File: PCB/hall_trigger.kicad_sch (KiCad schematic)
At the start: 2 parts

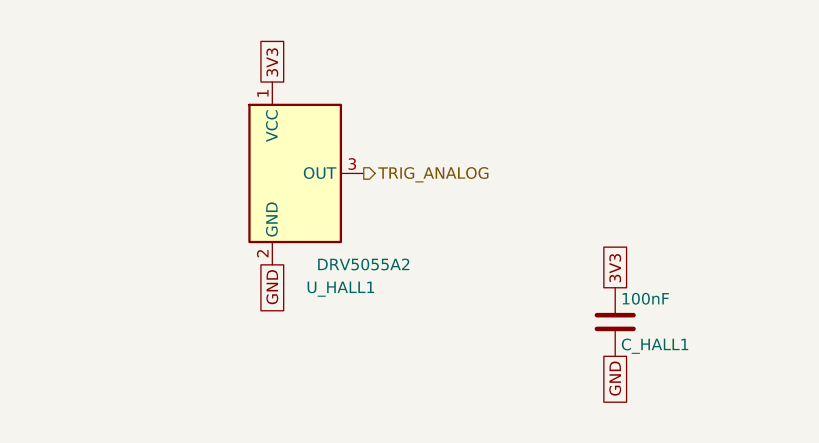
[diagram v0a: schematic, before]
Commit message: Fix footprints and begin layout (#17)
* refactor: updated gulikit footprint

This updates the gulikit thumbstick footprint to be accurate.

* layout: beginning pcb layout

This updates the schematic with a few different footprints while also starts the layout.
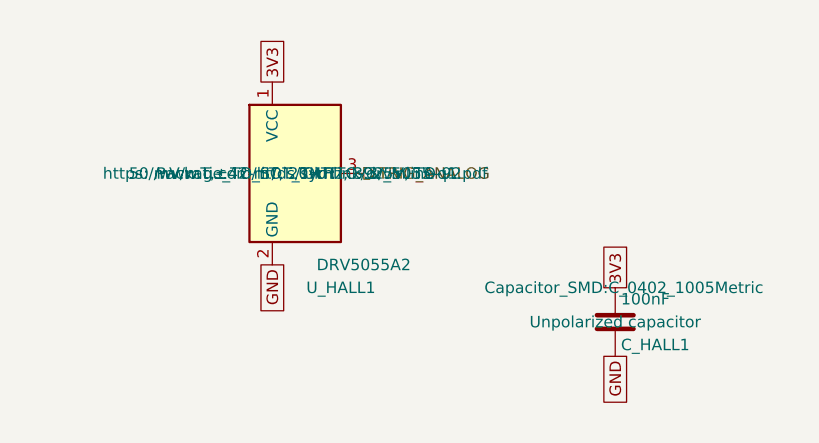
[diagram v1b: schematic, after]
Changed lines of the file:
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@@
 	(generator_version "10.0")
 	(paper "A4")
+	(global_label "3V3"
+		(shape passive)
+		(at 166.37 109.22 90)
+		(fields_autoplaced yes)
+		(effects
+			(font
+				(size 1.27 1.27)
+			)
+			(justify left)
+		)
+		(property "Intersheetrefs" "${INTERSHEET_REFS}"
+			(at 166.37 109.22 0)
+			(hide yes)
+			(show_name no)
+			(do_not_autoplace no)
+			(effects
+				(font
+					(size 1.27 1.27)
+				)
+			)
+		)
+	)
 	(global_label "GND"
 		(shape passive)
+		(at 128.27 106.68 270)
+		(fields_autoplaced yes)
+		(effects
+			(font
+				(size 1.27 1.27)
+			)
+			(justify right)
+		)
+		(property "Intersheetrefs" "${INTERSHEET_REFS}"
+			(at 128.27 106.68 0)
+			(hide yes)
+			(show_name no)
+			(do_not_autoplace no)
+			(effects
+				(font
+					(size 1.27 1.27)
+				)
+			)
+		)
+	)
+	(global_label "GND"
+		(shape passive)
 		(at 166.37 116.84 270)
 		(fields_autoplaced yes)
@@
 		(property "Intersheetrefs" "${INTERSHEET_REFS}"
 			(at 166.37 116.84 0)
-			(hide yes)
-			(show_name no)
-			(do_not_autoplace no)
-			(effects
-				(font
-					(size 1.27 1.27)
-				)
-			)
-		)
-	)
-	(global_label "3V3"
-		(shape passive)
-		(at 166.37 109.22 90)
-		(fields_autoplaced yes)
-		(effects
-			(font
-				(size 1.27 1.27)
-			)
-			(justify left)
-		)
-		(property "Intersheetrefs" "${INTERSHEET_REFS}"
-			(at 166.37 109.22 0)
-			(hide yes)
-			(show_name no)
-			(do_not_autoplace no)
-			(effects
-				(font
-					(size 1.27 1.27)
-				)
-			)
-		)
-	)
-	(global_label "GND"
-		(shape passive)
-		(at 128.27 106.68 270)
-		(fields_autoplaced yes)
-		(effects
-			(font
-				(size 1.27 1.27)
-			)
-			(justify right)
-		)
-		(property "Intersheetrefs" "${INTERSHEET_REFS}"
-			(at 128.27 106.68 0)
 			(hide yes)
 			(show_name no)
@@
 		(property "Footprint" "Capacitor_SMD:C_0402_1005Metric"
 			(at 167.3352 109.22 0)
-			(hide yes)
 			(show_name no)
 			(do_not_autoplace no)
@@
 		(property "Datasheet" ""
 			(at 166.37 113.03 0)
-			(hide yes)
 			(show_name no)
 			(do_not_autoplace no)
@@
 		(property "Description" "Unpolarized capacitor"
 			(at 166.37 113.03 0)
-			(hide yes)
 			(show_name no)
 			(do_not_autoplace no)
@@
 		(instances
 			(project "snips_controller"
-				(path "/868f8289-8434-4465-b2f4-2accc5e40bab/3b2478ec-2890-4ec8-b56f-d58b64ce58ab"
+				(path "/868f8289-8434-4465-b2f4-2accc5e40bab/58aa3fea-7023-42af-afb1-45eaa756099e"
 					(reference "C_HALL1")
+					(unit 1)
+				)
+			)
+			(project ""
+				(path "/d0f5b7d7-b2b6-4492-958c-e60265d3c6b4/58aa3fea-7023-42af-afb1-45eaa756099e"
+					(reference "C_HALL")
 					(unit 1)
 				)
@@
 		(property "Footprint" "Package_TO_SOT_THT:TO-92_Inline"
 			(at 130.81 96.52 0)
-			(hide yes)
 			(show_name no)
 			(do_not_autoplace no)
@@
 		(property "Datasheet" "https://www.ti.com/lit/ds/symlink/drv5055-q1.pdf"
 			(at 130.81 96.52 0)
-			(hide yes)
 			(show_name no)
 			(do_not_autoplace no)
@@
 		(property "Description" "50 mV/mT,±42-mT, 20-kHz, 3.3/5V, TO-92"
 			(at 130.81 96.52 0)
-			(hide yes)
 			(show_name no)
 			(do_not_autoplace no)
@@
 		(instances
 			(project "snips_controller"
-				(path "/868f8289-8434-4465-b2f4-2accc5e40bab/3b2478ec-2890-4ec8-b56f-d58b64ce58ab"
+				(path "/868f8289-8434-4465-b2f4-2accc5e40bab/58aa3fea-7023-42af-afb1-45eaa756099e"
 					(reference "U_HALL1")
 					(unit 1)
 				)
+			)
+			(project ""
+				(path "/d0f5b7d7-b2b6-4492-958c-e60265d3c6b4/58aa3fea-7023-42af-afb1-45eaa756099e"
+					(reference "U_HALL")
+					(unit 1)
+				)

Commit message: refactor: swap footprints and add symmetry
This updates the footprints of a couple components to be smaller and closer to what we want. It also adds two buttons to ensure left and right side symmetry.
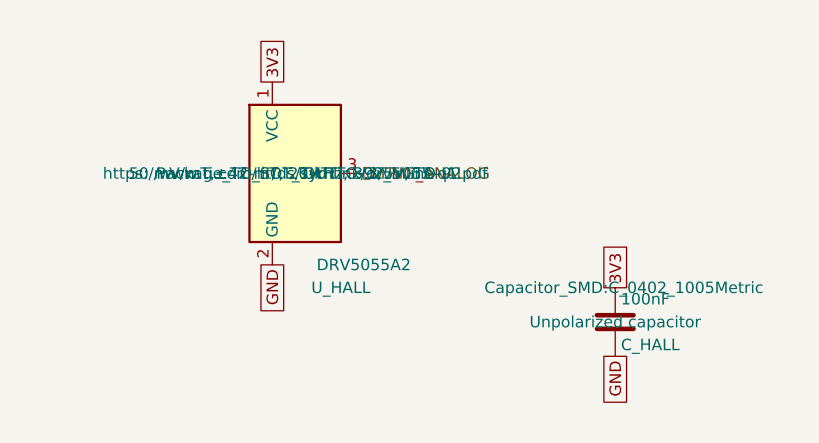
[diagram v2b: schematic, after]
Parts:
- removed C_HALL1: 100nF, Capacitor_SMD:C_0402_1005Metric, symbol Device:C
- removed U_HALL1: DRV5055A2, Package_TO_SOT_THT:TO-92_Inline, symbol Sensor_Magnetic:DRV5055A2xLPGxQ1
- added C_HALL: 100nF, Capacitor_SMD:C_0402_1005Metric, symbol Device:C
- added U_HALL: DRV5055A2, Package_TO_SOT_THT:TO-92_Inline, symbol Sensor_Magnetic:DRV5055A2xLPGxQ1
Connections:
- net 3V3: now also C_HALL.1, U_HALL.1 (VCC)
- net GND: now also C_HALL.2, U_HALL.2 (GND)
- net TRIG_ANALOG: now also U_HALL.3 (OUT)
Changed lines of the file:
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@@
 		(dnp no)
 		(fields_autoplaced yes)
-		(property "Reference" "C_HALL1"
+		(property "Reference" "C_HALL"
 			(at 167.005 115.57 0)
 			(show_name no)
@@
 		(instances
 			(project "snips_controller"
-				(path "/868f8289-8434-4465-b2f4-2accc5e40bab/58aa3fea-7023-42af-afb1-45eaa756099e"
-					(reference "C_HALL1")
-					(unit 1)
-				)
-			)
-			(project ""
-				(path "/d0f5b7d7-b2b6-4492-958c-e60265d3c6b4/58aa3fea-7023-42af-afb1-45eaa756099e"
+				(path "/f9d779c6-e1a6-4677-9004-6e9cc3d2fa8d/8effc149-159c-4301-a85e-5bb660fe4c99"
 					(reference "C_HALL")
 					(unit 1)
@@
 		(dnp no)
 		(fields_autoplaced yes)
-		(property "Reference" "U_HALL1"
+		(property "Reference" "U_HALL"
 			(at 135.89 109.22 0)
 			(show_name no)
@@
 		(instances
 			(project "snips_controller"
-				(path "/868f8289-8434-4465-b2f4-2accc5e40bab/58aa3fea-7023-42af-afb1-45eaa756099e"
-					(reference "U_HALL1")
-					(unit 1)
-				)
-			)
-			(project ""
-				(path "/d0f5b7d7-b2b6-4492-958c-e60265d3c6b4/58aa3fea-7023-42af-afb1-45eaa756099e"
+				(path "/f9d779c6-e1a6-4677-9004-6e9cc3d2fa8d/8effc149-159c-4301-a85e-5bb660fe4c99"
 					(reference "U_HALL")
 					(unit 1)

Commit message: layout: everything is on the board
The board edge cuts are down to 100mm x 35mm. All the components have the right footprints and are on the board, but no traces exist yet, and not all circuits are laid out properly yet. Lots of DRC warnings.
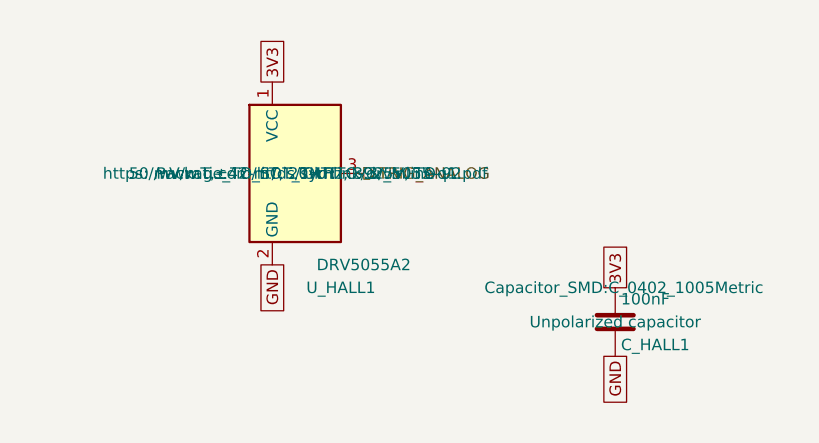
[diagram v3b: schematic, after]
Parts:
- removed C_HALL: 100nF, Capacitor_SMD:C_0402_1005Metric, symbol Device:C
- removed U_HALL: DRV5055A2, Package_TO_SOT_THT:TO-92_Inline, symbol Sensor_Magnetic:DRV5055A2xLPGxQ1
- added C_HALL1: 100nF, Capacitor_SMD:C_0402_1005Metric, symbol Device:C
- added U_HALL1: DRV5055A2, Package_TO_SOT_THT:TO-92_Inline, symbol Sensor_Magnetic:DRV5055A2xLPGxQ1
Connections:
- net 3V3: now also C_HALL1.1, U_HALL1.1 (VCC)
- net GND: now also C_HALL1.2, U_HALL1.2 (GND)
- net TRIG_ANALOG: now also U_HALL1.3 (OUT)
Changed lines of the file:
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@@
 	(generator_version "10.0")
 	(paper "A4")
+	(global_label "GND"
+		(shape passive)
+		(at 128.27 106.68 270)
+		(fields_autoplaced yes)
+		(effects
+			(font
+				(size 1.27 1.27)
+			)
+			(justify right)
+		)
+		(property "Intersheetrefs" "${INTERSHEET_REFS}"
+			(at 128.27 106.68 0)
+			(hide yes)
+			(show_name no)
+			(do_not_autoplace no)
+			(effects
+				(font
+					(size 1.27 1.27)
+				)
+			)
+		)
+	)
 	(global_label "3V3"
 		(shape passive)
@@
 		(property "Intersheetrefs" "${INTERSHEET_REFS}"
 			(at 166.37 109.22 0)
-			(hide yes)
-			(show_name no)
-			(do_not_autoplace no)
-			(effects
-				(font
-					(size 1.27 1.27)
-				)
-			)
-		)
-	)
-	(global_label "GND"
-		(shape passive)
-		(at 128.27 106.68 270)
-		(fields_autoplaced yes)
-		(effects
-			(font
-				(size 1.27 1.27)
-			)
-			(justify right)
-		)
-		(property "Intersheetrefs" "${INTERSHEET_REFS}"
-			(at 128.27 106.68 0)
 			(hide yes)
 			(show_name no)
@@
 			)
 			(justify left)
+		)
+	)
+	(symbol
+		(lib_id "Sensor_Magnetic:DRV5055A2xLPGxQ1")
+		(at 130.81 96.52 0)
+		(unit 1)
+		(body_style 1)
+		(exclude_from_sim no)
+		(in_bom yes)
+		(on_board yes)
+		(in_pos_files yes)
+		(dnp no)
+		(fields_autoplaced yes)
+		(property "Reference" "U_HALL1"
+			(at 135.89 109.22 0)
+			(show_name no)
+			(do_not_autoplace no)
+			(effects
+				(font
+					(size 1.27 1.27)
+				)
+			)
+		)
+		(property "Value" "DRV5055A2"
+			(at 138.43 106.68 0)
+			(show_name no)
+			(do_not_autoplace no)
+			(effects
+				(font
+					(size 1.27 1.27)
+				)
+			)
+		)
+		(property "Footprint" "Package_TO_SOT_THT:TO-92_Inline"
+			(at 130.81 96.52 0)
+			(show_name no)
+			(do_not_autoplace no)
+			(effects
+				(font
+					(size 1.27 1.27)
+				)
+			)
+		)
+		(property "Datasheet" "https://www.ti.com/lit/ds/symlink/drv5055-q1.pdf"
+			(at 130.81 96.52 0)
+			(show_name no)
+			(do_not_autoplace no)
+			(effects
+				(font
+					(size 1.27 1.27)
+				)
+			)
+		)
+		(property "Description" "50 mV/mT,±42-mT, 20-kHz, 3.3/5V, TO-92"
+			(at 130.81 96.52 0)
+			(show_name no)
+			(do_not_autoplace no)
+			(effects
+				(font
+					(size 1.27 1.27)
+				)
+			)
+		)
+		(pin "1"
+		)
+		(pin "2"
+		)
+		(pin "3"
+		)
+		(instances
+			(project "snips_controller"
+				(path "/21935953-32a0-46ad-8079-8177920c6978/15cccc75-ae28-44d0-aa53-203a86ee0065"
+					(reference "U_HALL1")
+					(unit 1)
+				)
+			)
 		)
 	)
@@
 		(dnp no)
 		(fields_autoplaced yes)
-		(property "Reference" "C_HALL"
+		(property "Reference" "C_HALL1"
 			(at 167.005 115.57 0)
 			(show_name no)
@@
 		(instances
 			(project "snips_controller"
-				(path "/f9d779c6-e1a6-4677-9004-6e9cc3d2fa8d/8effc149-159c-4301-a85e-5bb660fe4c99"
-					(reference "C_HALL")
+				(path "/21935953-32a0-46ad-8079-8177920c6978/15cccc75-ae28-44d0-aa53-203a86ee0065"
+					(reference "C_HALL1")
 					(unit 1)
 				)
-			)
-		)
-	)
-	(symbol
-		(lib_id "Sensor_Magnetic:DRV5055A2xLPGxQ1")
-		(at 130.81 96.52 0)
-		(unit 1)
-		(body_style 1)
-		(exclude_from_sim no)
-		(in_bom yes)
-		(on_board yes)
-		(in_pos_files yes)
-		(dnp no)
-		(fields_autoplaced yes)
-		(property "Reference" "U_HALL"
-			(at 135.89 109.22 0)
-			(show_name no)
-			(do_not_autoplace no)
-			(effects
-				(font
-					(size 1.27 1.27)
-				)
-			)
-		)
-		(property "Value" "DRV5055A2"
-			(at 138.43 106.68 0)
-			(show_name no)
-			(do_not_autoplace no)
-			(effects
-				(font
-					(size 1.27 1.27)
-				)
-			)
-		)
-		(property "Footprint" "Package_TO_SOT_THT:TO-92_Inline"
-			(at 130.81 96.52 0)
-			(show_name no)
-			(do_not_autoplace no)
-			(effects
-				(font
-					(size 1.27 1.27)
-				)
-			)
-		)
-		(property "Datasheet" "https://www.ti.com/lit/ds/symlink/drv5055-q1.pdf"
-			(at 130.81 96.52 0)
-			(show_name no)
-			(do_not_autoplace no)
-			(effects
-				(font
-					(size 1.27 1.27)
-				)
-			)
-		)
-		(property "Description" "50 mV/mT,±42-mT, 20-kHz, 3.3/5V, TO-92"
-			(at 130.81 96.52 0)
-			(show_name no)
-			(do_not_autoplace no)
-			(effects
-				(font
-					(size 1.27 1.27)
-				)
-			)
-		)
-		(pin "1"
-		)
-		(pin "2"
-		)
-		(pin "3"
-		)
-		(instances
-			(project "snips_controller"
-				(path "/f9d779c6-e1a6-4677-9004-6e9cc3d2fa8d/8effc149-159c-4301-a85e-5bb660fe4c99"
-					(reference "U_HALL")
-					(unit 1)
-				)

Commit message: task: part number populated (#26)
kicad-happy run part 2 - MPN numbers populated
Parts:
- C_HALL1: MF (none) -> Yageo; Manufacturer_Part_Number (none) -> CC0402KRX7R9BB104
- U_HALL1: MF (none) -> Texas Instruments; Manufacturer_Part_Number (none) -> DRV5055A2QLPGM
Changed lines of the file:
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@@
+			)
+		)
+		(property "MF" "Texas Instruments" (at 0 0 0)
+			(effects
+				(font
+					(size 1.27 1.27)
+				)
+				(hide yes)
+			)
+		)
+		(property "Manufacturer_Part_Number" "DRV5055A2QLPGM" (at 0 0 0)
+			(effects
+				(font
+					(size 1.27 1.27)
+				)
+				(hide yes)
 			)
 		)
@@
 			)
 		)
+		(property "MF" "Yageo" (at 0 0 0)
+			(effects
+				(font
+					(size 1.27 1.27)
+				)
+				(hide yes)
+			)
+		)
+		(property "Manufacturer_Part_Number" "CC0402KRX7R9BB104" (at 0 0 0)
+			(effects
+				(font
+					(size 1.27 1.27)
+				)
+				(hide yes)
+			)
+		)

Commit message: task: generate production files (#27)
* task: generate production files

We have wrapped up board validation. Gerbers are now generated. Logo generated. Good to go.

* refactor: added STAT2

It was worth adding and will give us more info during battery charging.
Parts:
- U_HALL1: now left out of the parts list
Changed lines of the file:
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@@
 		(body_style 1)
 		(exclude_from_sim no)
-		(in_bom yes)
+		(in_bom no)
 		(on_board yes)
 		(in_pos_files yes)
@@
 			)
 		)
-		(property "MF" "Texas Instruments" (at 0 0 0)
+		(property "MF" "Texas Instruments"
+			(at 0 0 0)
+			(hide yes)
+			(show_name no)
+			(do_not_autoplace no)
 			(effects
 				(font
 					(size 1.27 1.27)
 				)
-				(hide yes)
 			)
 		)
-		(property "Manufacturer_Part_Number" "DRV5055A2QLPGM" (at 0 0 0)
+		(property "Manufacturer_Part_Number" "DRV5055A2QLPGM"
+			(at 0 0 0)
+			(hide yes)
+			(show_name no)
+			(do_not_autoplace no)
 			(effects
 				(font
 					(size 1.27 1.27)
 				)
-				(hide yes)
 			)
 		)
@@
 			)
 		)
-		(property "MF" "Yageo" (at 0 0 0)
+		(property "MF" "Yageo"
+			(at 0 0 0)
+			(hide yes)
+			(show_name no)
+			(do_not_autoplace no)
 			(effects
 				(font
 					(size 1.27 1.27)
 				)
-				(hide yes)
 			)
 		)
-		(property "Manufacturer_Part_Number" "CC0402KRX7R9BB104" (at 0 0 0)
+		(property "Manufacturer_Part_Number" "CC0402KRX7R9BB104"
+			(at 0 0 0)
+			(hide yes)
+			(show_name no)
+			(do_not_autoplace no)
 			(effects
 				(font
 					(size 1.27 1.27)
 				)
-				(hide yes)
 			)
 		)
